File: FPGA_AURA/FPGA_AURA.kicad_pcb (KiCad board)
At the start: 2 copper layers, 50 x 50 mm, 1 part, among them U1 XC7A35T-2FTG256C

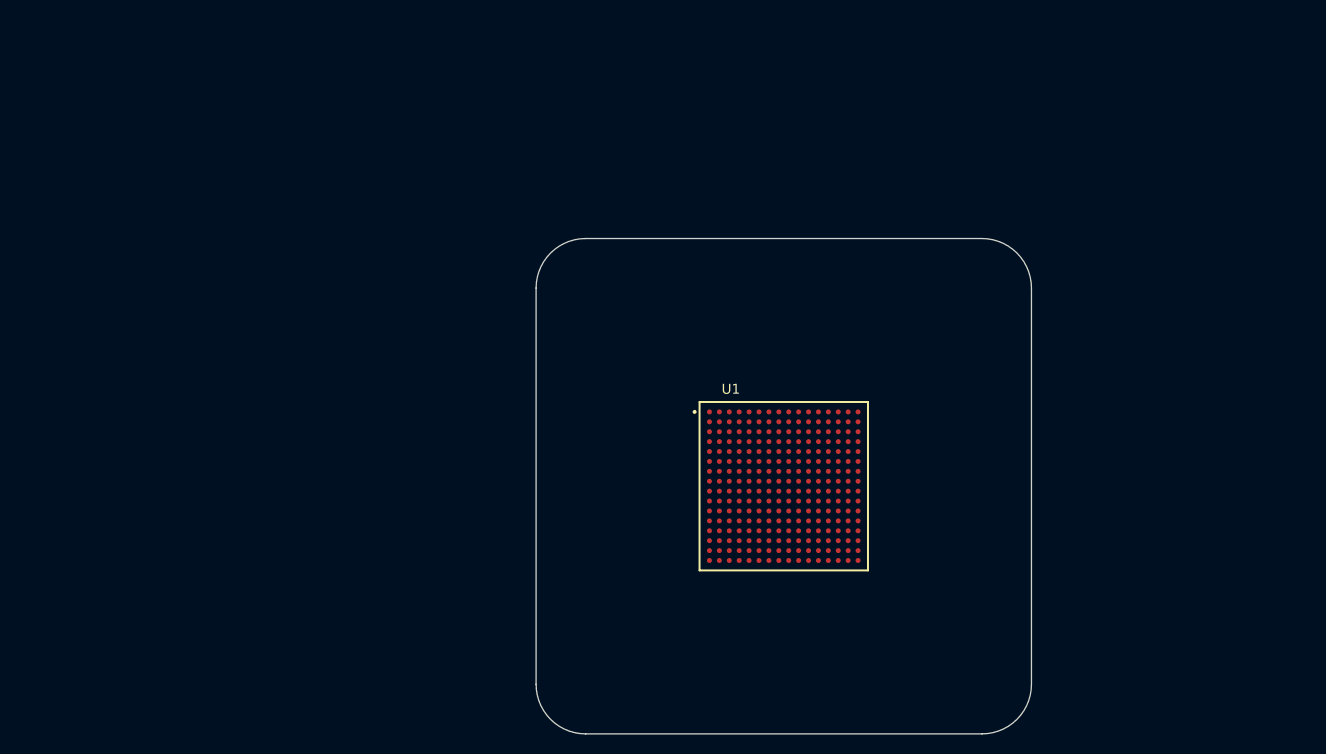
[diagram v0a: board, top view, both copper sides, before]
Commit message: Power regulation started
Started doing research into the project to see what needs to be done
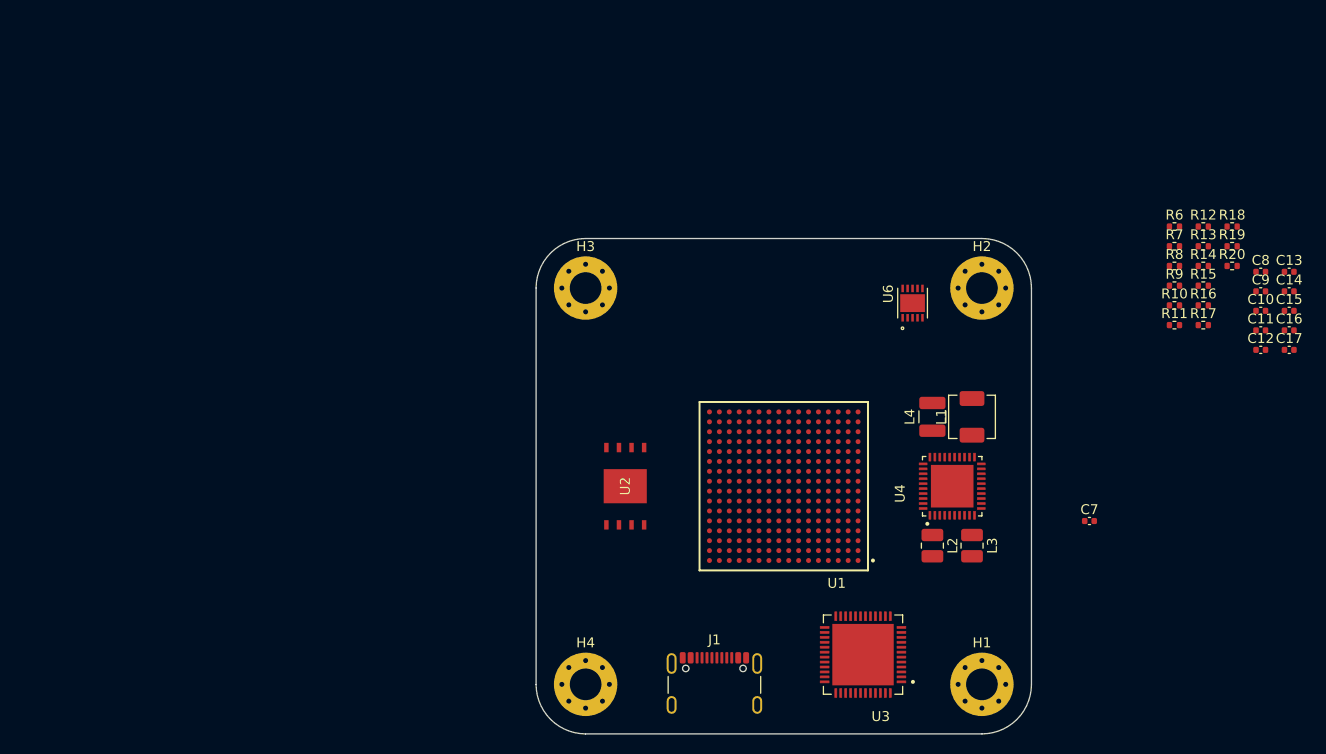
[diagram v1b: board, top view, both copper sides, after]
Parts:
- added C10: 4u7, Capacitor_SMD:C_0402_1005Metric, F.Cu at (173.1, 57.3)
- added C11: 470n, Capacitor_SMD:C_0402_1005Metric, F.Cu at (173.1, 59.3)
- added C12: 470n, Capacitor_SMD:C_0402_1005Metric, F.Cu at (173.1, 61.2)
- added C13: 22u, Capacitor_SMD:C_0402_1005Metric, F.Cu at (176.0, 53.4)
- added C14: 22u, Capacitor_SMD:C_0402_1005Metric, F.Cu at (176.0, 55.3)
- added C15: 4u7, Capacitor_SMD:C_0402_1005Metric, F.Cu at (176.0, 57.3)
- added C16: 10u, Capacitor_SMD:C_0402_1005Metric, F.Cu at (176.0, 59.3)
- added C17: 10u, Capacitor_SMD:C_0402_1005Metric, F.Cu at (176.0, 61.2)
- added C7: 470n, Capacitor_SMD:C_0402_1005Metric, F.Cu at (155.9, 78.5)
- added C8: 10n, Capacitor_SMD:C_0402_1005Metric, F.Cu at (173.1, 53.4)
- added C9: 100n, Capacitor_SMD:C_0402_1005Metric, F.Cu at (173.1, 55.3)
- added H1: MountingHole_Pad, MountingHole:MountingHole_3.2mm_M3_Pad_Via, F.Cu at (145.0, 95.0)
- added H2: MountingHole_Pad, MountingHole:MountingHole_3.2mm_M3_Pad_Via, F.Cu at (145.0, 55.0)
- added H3: MountingHole_Pad, MountingHole:MountingHole_3.2mm_M3_Pad_Via, F.Cu at (105.0, 55.0)
- added H4: MountingHole_Pad, MountingHole:MountingHole_3.2mm_M3_Pad_Via, F.Cu at (105.0, 95.0)
- added J1: USB_C_Receptacle_USB2.0_16P, Connector_USB:USB_C_Receptacle_GCT_USB4105-xx-A_16P_TopMnt_Horizontal, F.Cu at (118.0, 96.0)
- added L1: 1u, Inductor_SMD:L_Changjiang_FXL0420, F.Cu at (144.0, 68.0)
- added L2: 1u5, Inductor_SMD:L_1008_2520Metric, F.Cu at (140.0, 81.0)
- added L3: 2u2, Inductor_SMD:L_1008_2520Metric, F.Cu at (144.0, 81.0)
- added L4: 680n, Inductor_SMD:L_1210_3225Metric, F.Cu at (140.0, 68.0)
- added R10: 47k, Resistor_SMD:R_0402_1005Metric, F.Cu at (164.4, 56.8)
- added R11: 0R, Resistor_SMD:R_0402_1005Metric, F.Cu at (164.4, 58.7)
- added R12: 1k, Resistor_SMD:R_0402_1005Metric, F.Cu at (167.3, 48.8)
- added R13: 10k, Resistor_SMD:R_0402_1005Metric, F.Cu at (167.3, 50.8)
- added R14: 10k, Resistor_SMD:R_0402_1005Metric, F.Cu at (167.3, 52.8)
- added R15: 22k, Resistor_SMD:R_0402_1005Metric, F.Cu at (167.3, 54.8)
- added R16: 31k6, Resistor_SMD:R_0402_1005Metric, F.Cu at (167.3, 56.8)
- added R17: 0R, Resistor_SMD:R_0402_1005Metric, F.Cu at (167.3, 58.7)
- added R18: 10k, Resistor_SMD:R_0402_1005Metric, F.Cu at (170.3, 48.8)
- added R19: 10k, Resistor_SMD:R_0402_1005Metric, F.Cu at (170.3, 50.8)
- added R20: 15k, Resistor_SMD:R_0402_1005Metric, F.Cu at (170.3, 52.8)
- added R6: 10k, Resistor_SMD:R_0402_1005Metric, F.Cu at (164.4, 48.8)
- added R7: 10k, Resistor_SMD:R_0402_1005Metric, F.Cu at (164.4, 50.8)
- added R8: 10k, Resistor_SMD:R_0402_1005Metric, F.Cu at (164.4, 52.8)
- added R9: 10k, Resistor_SMD:R_0402_1005Metric, F.Cu at (164.4, 54.8)
- added U2: W25Q256JVEIQ, W25Q256JVEIQ:SON127P800X600X80-9N, F.Cu at (109.0, 75.0)
- added U3: FT232HQ-REEL, FT232HQ-REEL:QFN50P800X800X90-49N, F.Cu at (133.0, 92.0)
- added U4: ADP5014, ADP5014ACPZ-R7:QFN50P600X600X80-41N430X430, F.Cu at (142.0, 75.0)
- added U6: NCP51200MNTXG, NCP51200MNTXG:SON50P300X300X100-11N, F.Cu at (138.0, 56.5)
- turned U1 to 180 degrees
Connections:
- U1 pad A1: unconnected-(U1A-GND-PadA1) -> GND
- U1 pad A11: unconnected-(U1A-GND-PadA11) -> GND
- U1 pad A16: unconnected-(U1A-VCCO_15-PadA16) -> +3V3
- U1 pad A6: unconnected-(U1A-VCCO_35-PadA6) -> +3V3
- U1 pad B13: unconnected-(U1A-VCCO_15-PadB13) -> +3V3
- U1 pad B3: unconnected-(U1A-VCCO_35-PadB3) -> +3V3
- U1 pad B8: unconnected-(U1A-GND-PadB8) -> GND
- U1 pad C10: unconnected-(U1A-VCCO_15-PadC10) -> +3V3
- U1 pad C15: unconnected-(U1A-GND-PadC15) -> GND
- U1 pad C5: unconnected-(U1A-GND-PadC5) -> GND
- U1 pad D12: unconnected-(U1A-GND-PadD12) -> GND
- U1 pad D2: unconnected-(U1A-GND-PadD2) -> GND
- U1 pad D7: unconnected-(U1A-VCCO_35-PadD7) -> +3V3
- U1 pad E10: unconnected-(U1A-VCCBRAM-PadE10) -> +1V0
- U1 pad E14: unconnected-(U1A-VCCO_15-PadE14) -> +3V3
- U1 pad E4: unconnected-(U1A-VCCO_35-PadE4) -> +3V3
- U1 pad E8: unconnected-(U1A-CCLK_0-PadE8) -> Net-(U1A-CCLK_0)
- U1 pad E9: unconnected-(U1A-GND-PadE9) -> GND
- U1 pad F1: unconnected-(U1A-VCCO_35-PadF1) -> +3V3
- U1 pad F10: unconnected-(U1A-GND-PadF10) -> GND
- U1 pad F11: unconnected-(U1A-VCCBRAM-PadF11) -> +1V0
- U1 pad F16: unconnected-(U1A-GND-PadF16) -> GND
- U1 pad F6: unconnected-(U1A-GND-PadF6) -> GND
- U1 pad F7: unconnected-(U1A-VCCINT-PadF7) -> +1V0
- U1 pad F8: unconnected-(U1A-VCCBATT_0-PadF8) -> GND
- U1 pad F9: unconnected-(U1A-VCCINT-PadF9) -> +1V0
- U1 pad G10: unconnected-(U1A-VCCAUX-PadG10) -> +1V8
- U1 pad G13: unconnected-(U1A-GND-PadG13) -> GND
- U1 pad G3: unconnected-(U1A-GND-PadG3) -> GND
- U1 pad G6: unconnected-(U1A-VCCINT-PadG6) -> +1V0
- U1 pad G7: unconnected-(U1A-GNDADC_0-PadG7) -> GND
- U1 pad G9: unconnected-(U1A-GND-PadG9) -> GND
- U1 pad H15: unconnected-(U1A-VCCO_15-PadH15) -> +3V3
- U1 pad H6: unconnected-(U1A-GND-PadH6) -> GND
- U1 pad H7: unconnected-(U1A-VREFN_0-PadH7) -> GND
- U1 pad H9: unconnected-(U1A-VCCINT-PadH9) -> +1V0
- U1 pad J10: unconnected-(U1A-VCCAUX-PadJ10) -> +1V8
- U1 pad J11: unconnected-(U1A-GND-PadJ11) -> GND
- U1 pad J12: unconnected-(U1A-VCCO_15-PadJ12) -> +3V3
- U1 pad J2: unconnected-(U1A-VCCO_35-PadJ2) -> +3V3
- U1 pad J6: unconnected-(U1A-VCCINT-PadJ6) -> +1V0
- U1 pad J9: unconnected-(U1A-GND-PadJ9) -> GND
- U1 pad K11: unconnected-(U1A-VCCAUX-PadK11) -> +1V8
- U1 pad K14: unconnected-(U1A-GND-PadK14) -> GND
- U1 pad K15: unconnected-(U1A-IO_L2P_T0_D02_14-PadK15) -> Net-(U1A-IO_L2P_T0_D02_14)
- U1 pad K16: unconnected-(U1A-IO_L2N_T0_D03_14-PadK16) -> Net-(U1A-IO_L2N_T0_D03_14)
- U1 pad K4: unconnected-(U1A-GND-PadK4) -> GND
- U1 pad K6: unconnected-(U1A-GND-PadK6) -> GND
- U1 pad K9: unconnected-(U1A-VCCINT-PadK9) -> +1V0
- U1 pad L1: unconnected-(U1A-GND-PadL1) -> GND
- U1 pad L10: unconnected-(U1A-VCCAUX-PadL10) -> +1V8
- U1 pad L11: unconnected-(U1A-GND-PadL11) -> GND
- U1 pad L12: unconnected-(U1A-IO_L6P_T0_FCS_B_14-PadL12) -> Net-(U1A-IO_L6P_T0_FCS_B_14)
- U1 pad L16: unconnected-(U1A-VCCO_14-PadL16) -> +3V3
- U1 pad L8: unconnected-(U1A-VCCINT-PadL8) -> +1V0
- U1 pad M13: unconnected-(U1A-VCCO_14-PadM13) -> +3V3
- U1 pad M3: unconnected-(U1A-VCCO_34-PadM3) -> +3V3
- U1 pad M8: unconnected-(U1A-GND-PadM8) -> GND
- U1 pad N10: unconnected-(U1A-VCCO_14-PadN10) -> +3V3
- U1 pad N15: unconnected-(U1A-GND-PadN15) -> GND
- U1 pad N5: unconnected-(U1A-GND-PadN5) -> GND
- U1 pad P12: unconnected-(U1A-GND-PadP12) -> GND
- U1 pad P2: unconnected-(U1A-GND-PadP2) -> GND
- U1 pad P7: unconnected-(U1A-VCCO_14-PadP7) -> +3V3
- U1 pad R14: unconnected-(U1A-VCCO_14-PadR14) -> +3V3
- U1 pad R4: unconnected-(U1A-VCCO_34-PadR4) -> +3V3
- U1 pad R9: unconnected-(U1A-GND-PadR9) -> GND
- U1 pad T1: unconnected-(U1A-VCCO_34-PadT1) -> +3V3
- U1 pad T11: unconnected-(U1A-VCCO_14-PadT11) -> +3V3
- U1 pad T16: unconnected-(U1A-GND-PadT16) -> GND
- U1 pad T6: unconnected-(U1A-GND-PadT6) -> GND

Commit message: Initial component selection done
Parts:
- removed C10, C15: 4u7, Capacitor_SMD:C_0402_1005Metric
- removed C11, C12, C7: 470n, Capacitor_SMD:C_0402_1005Metric
- removed C13, C14: 22u, Capacitor_SMD:C_0402_1005Metric
- removed C16, C17: 10u, Capacitor_SMD:C_0402_1005Metric
- removed C8: 10n, Capacitor_SMD:C_0402_1005Metric
- removed C9: 100n, Capacitor_SMD:C_0402_1005Metric
- removed L1: 1u, Inductor_SMD:L_Changjiang_FXL0420
- removed L2: 1u5, Inductor_SMD:L_1008_2520Metric
- removed L3: 2u2, Inductor_SMD:L_1008_2520Metric
- removed L4: 680n, Inductor_SMD:L_1210_3225Metric
- removed R10: 47k, Resistor_SMD:R_0402_1005Metric
- removed R11, R17: 0R, Resistor_SMD:R_0402_1005Metric
- removed R12: 1k, Resistor_SMD:R_0402_1005Metric
- removed R13, R14, R18, R19, R6, R7, R8, R9: 10k, Resistor_SMD:R_0402_1005Metric
- removed R15: 22k, Resistor_SMD:R_0402_1005Metric
- removed R16: 31k6, Resistor_SMD:R_0402_1005Metric
- removed R20: 15k, Resistor_SMD:R_0402_1005Metric
- removed U4: ADP5014, ADP5014ACPZ-R7:QFN50P600X600X80-41N430X430
- removed U6: NCP51200MNTXG, NCP51200MNTXG:SON50P300X300X100-11N
- added C200: 10u, Capacitor_SMD:C_0603_1608Metric, F.Cu at (145.8, 80.8)
- added C201: 10u, Capacitor_SMD:C_0603_1608Metric, F.Cu at (140.2, 80.8)
- added C202: 10u, Capacitor_SMD:C_0603_1608Metric, F.Cu at (147.0, 70.8)
- added C203: 10u, Capacitor_SMD:C_0603_1608Metric, F.Cu at (139.2, 70.8)
- added C205: 470n, Capacitor_SMD:C_0402_1005Metric, F.Cu at (138.0, 76.5)
- added C206: 47u, Capacitor_SMD:C_0805_2012Metric, F.Cu at (141.2, 62.0)
- added C207: 47u, Capacitor_SMD:C_0805_2012Metric, F.Cu at (144.8, 62.0)
- added C208: 47u, Capacitor_SMD:C_0805_2012Metric, F.Cu at (141.2, 86.5)
- added C209: 47u, Capacitor_SMD:C_0805_2012Metric, F.Cu at (144.8, 86.5)
- added C210: 3n6, Capacitor_SMD:C_0402_1005Metric, F.Cu at (138.0, 72.0)
- added C211: 8n, Capacitor_SMD:C_0402_1005Metric, F.Cu at (148.0, 72.5)
- added C212: 2n2, Capacitor_SMD:C_0402_1005Metric, F.Cu at (138.0, 79.5)
- added C213: 5n, Capacitor_SMD:C_0402_1005Metric, F.Cu at (148.0, 79.5)
- added C214: 4u7, Capacitor_SMD:C_0402_1005Metric, F.Cu at (136.5, 61.5)
- added C215: 22u, Capacitor_SMD:C_0402_1005Metric, F.Cu at (135.8, 54.2)
- added C216: 470n, Capacitor_SMD:C_0402_1005Metric, F.Cu at (133.8, 54.2)
- added C217: 470n, Capacitor_SMD:C_0402_1005Metric, F.Cu at (134.8, 54.2)
- added C218: 10n, Capacitor_SMD:C_0402_1005Metric, F.Cu at (138.0, 56.2)
- added C219: 100n, Capacitor_SMD:C_0402_1005Metric, F.Cu at (133.5, 61.5)
- added C220: 1u, Capacitor_SMD:C_0402_1005Metric, F.Cu at (138.0, 74.0)
- added J101: XT30PW-M, XT30PWM:XT30PWM, F.Cu at (132.0, 92.8)
- added L200: 680n, Inductor_SMD:L_Chilisin_BMRB00050518-B, F.Cu at (139.5, 66.5)
- added L201: 1u, Inductor_SMD:L_Chilisin_BMRB00050518-B, F.Cu at (146.5, 66.5)
- added L202: 1u5, Inductor_SMD:L_1008_2520Metric, F.Cu at (141.0, 83.5)
- added L203: 2u2, Inductor_SMD:L_1008_2520Metric, F.Cu at (145.0, 83.5)
- added R200: 27k, Resistor_SMD:R_0402_1005Metric, B.Cu at (140.5, 74.5)
- added R201: 4k9, Resistor_SMD:R_0402_1005Metric, B.Cu at (140.5, 75.5)
- added R202: 0R, Resistor_SMD:R_0402_1005Metric, B.Cu at (140.5, 73.2)
- added R203: 56k2, Resistor_SMD:R_0402_1005Metric, B.Cu at (140.5, 77.0)
- added R204: 0R, Resistor_SMD:R_0402_1005Metric, F.Cu at (148.0, 75.2)
- added R205: 31k6, Resistor_SMD:R_0402_1005Metric, F.Cu at (148.0, 76.2)
- added R206: 100k, Resistor_SMD:R_0402_1005Metric, F.Cu at (138.0, 75.0)
- added R207: 10k, Resistor_SMD:R_0402_1005Metric, F.Cu at (136.2, 74.8)
- added R208: 10k, Resistor_SMD:R_0402_1005Metric, F.Cu at (135.2, 74.8)
- added R209: 1k, Resistor_SMD:R_0402_1005Metric, F.Cu at (136.2, 76.8)
- added R210: 10k, Resistor_SMD:R_0402_1005Metric, F.Cu at (135.2, 76.8)
- added R211: 10k, Resistor_SMD:R_0402_1005Metric, F.Cu at (138.0, 77.5)
- added R212: 22k, Resistor_SMD:R_0402_1005Metric, F.Cu at (138.0, 78.5)
- added R213: 10k, Resistor_SMD:R_0402_1005Metric, F.Cu at (148.0, 78.2)
- added R214: 15k, Resistor_SMD:R_0402_1005Metric, F.Cu at (148.0, 77.2)
- added R215: 2k7, Resistor_SMD:R_0402_1005Metric, F.Cu at (138.0, 73.0)
- added R216: 2k7, Resistor_SMD:R_0402_1005Metric, F.Cu at (148.0, 73.5)
- added R217: 5k6, Resistor_SMD:R_0402_1005Metric, F.Cu at (140.0, 79.5)
- added R218: 9k1, Resistor_SMD:R_0402_1005Metric, F.Cu at (146.0, 79.5)
- added R219: 47k, Resistor_SMD:R_0402_1005Metric, B.Cu at (141.8, 78.2)
- added R220: 0R, Resistor_SMD:R_0402_1005Metric, F.Cu at (134.5, 61.5)
- added R221: 10k, Resistor_SMD:R_0402_1005Metric, F.Cu at (138.0, 58.2)
- added R222: 10k, Resistor_SMD:R_0402_1005Metric, F.Cu at (138.0, 57.2)
- added R223: 47k, Resistor_SMD:R_0402_1005Metric, F.Cu at (135.5, 61.5)
- added U200: ADP5014, ADP5014ACPZ-R7:QFN50P600X600X80-41N430X430, F.Cu at (143.0, 75.2)
- added U201: NCP51200MNTXG, NCP51200MNTXG:SON50P300X300X100-11N, F.Cu at (135.0, 58.0)
- added U500: MT41K128M16JT-125_IT_K, MT41K128M16JT-125_IT_K:BGA80P96C6X16_800X1400X110, F.Cu at (125.0, 58.0)
- moved U3 26.9 mm to (108.0, 82.0)
- moved U2 7.07 mm to (108.0, 68.0)
- moved J1 0.30 mm to (118.0, 96.3)
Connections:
- U1 pad E8: Net-(U1A-CCLK_0) -> unconnected-(U1A-CCLK_0-PadE8)
- U1 pad K15: Net-(U1A-IO_L2P_T0_D02_14) -> unconnected-(U1A-IO_L2P_T0_D02_14-PadK15)
- U1 pad K16: Net-(U1A-IO_L2N_T0_D03_14) -> unconnected-(U1A-IO_L2N_T0_D03_14-PadK16)
- U1 pad L12: Net-(U1A-IO_L6P_T0_FCS_B_14) -> unconnected-(U1A-IO_L6P_T0_FCS_B_14-PadL12)
- U2 pad 1: Net-(U1A-IO_L6P_T0_FCS_B_14) -> unconnected-(U2-/CS-Pad1)
- U2 pad 6: Net-(U1A-CCLK_0) -> unconnected-(U2-CLK-Pad6)
- U2 pad 7: Net-(U1A-IO_L2N_T0_D03_14) -> unconnected-(U2-/HOLD-Pad7)
- U2 pad 9: Net-(U1A-IO_L2P_T0_D02_14) -> unconnected-(U2-/WP-Pad9)
